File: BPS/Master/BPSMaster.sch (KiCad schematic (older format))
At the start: 21 parts, among them J1 SWD, J13 CAN Analyzer, J5 SPI Analyzer, SW1 B3SL-1002P, U1 STM32F413RHTx, Y1 8M

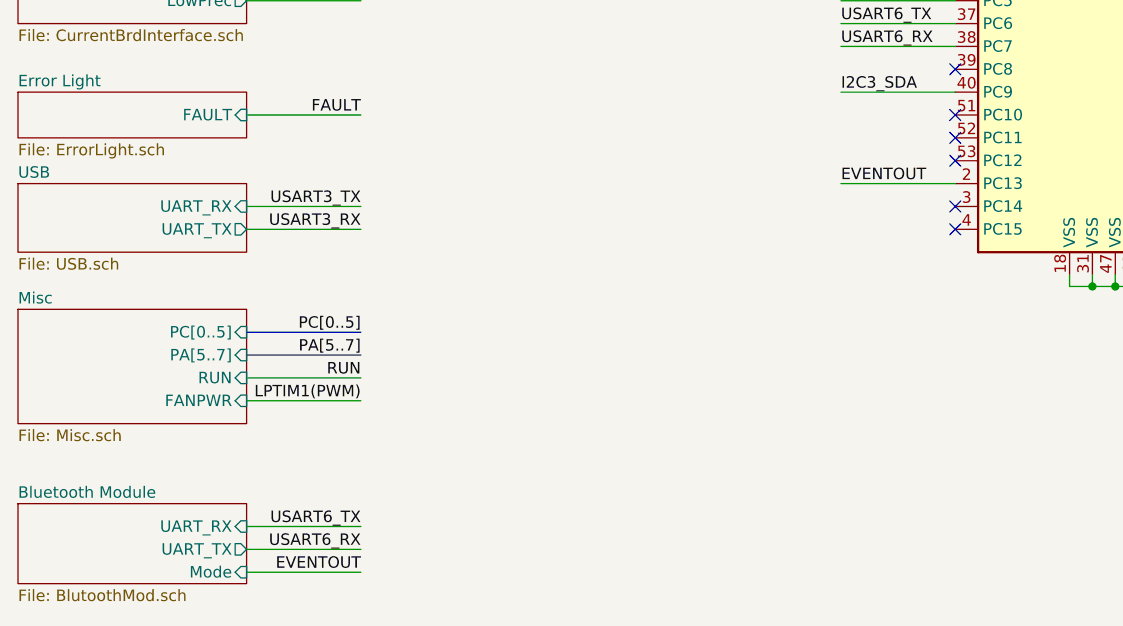
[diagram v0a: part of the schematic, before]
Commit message: The setup for bluetooth mode can't be done through a port using the STM so I used a switch instead, we can use that to toggle between Application mode and testing mode.
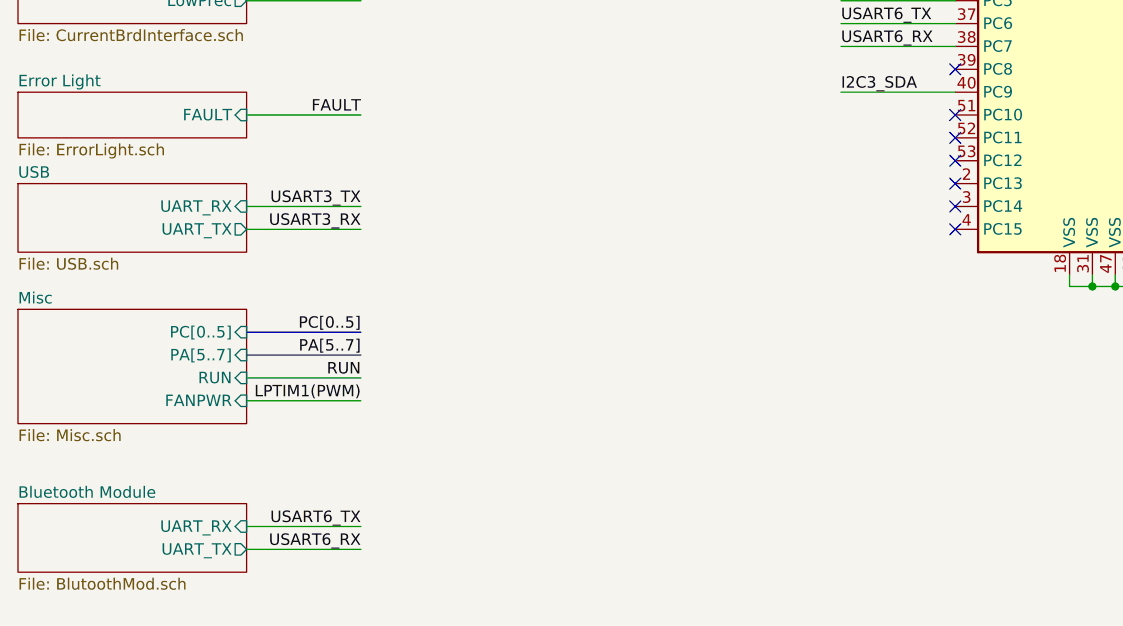
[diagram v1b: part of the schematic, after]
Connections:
- net EVENTOUT: no longer names the net of U1.2 (PC13)
- no-connect marks 19 -> 20
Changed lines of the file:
@@
 USART6_RX
 $Sheet
-S 1000 6700 1000 350
+S 1000 6700 1000 300
 U 5EE39517
 F0 "Bluetooth Module" 50
@@
 F2 "UART_RX" I R 2000 6800 50
 F3 "UART_TX" O R 2000 6900 50
-F4 "Mode" I R 2000 7000 50
 $EndSheet
 Wire Wire Line
@@
 Wire Wire Line
 	2000 6800 2500 6800
-Wire Wire Line
-	2000 7000 2500 7000
 Text Label 2500 6900 2    50   ~ 0
 USART6_RX
 Text Label 2500 6800 2    50   ~ 0
 USART6_TX
-Wire Wire Line
-	5100 5300 4600 5300
-Text Label 4600 5300 0    50   ~ 0
-EVENTOUT
-Text Label 2500 7000 2    50   ~ 0
-EVENTOUT
 Wire Wire Line
 	5100 4600 4600 4600
@@
 Text Label 2500 6250 2    50   ~ 0
 LPTIM1(PWM)
+NoConn ~ 5100 5300
 Wire Bus Line
 	7100 2700 7100 3000

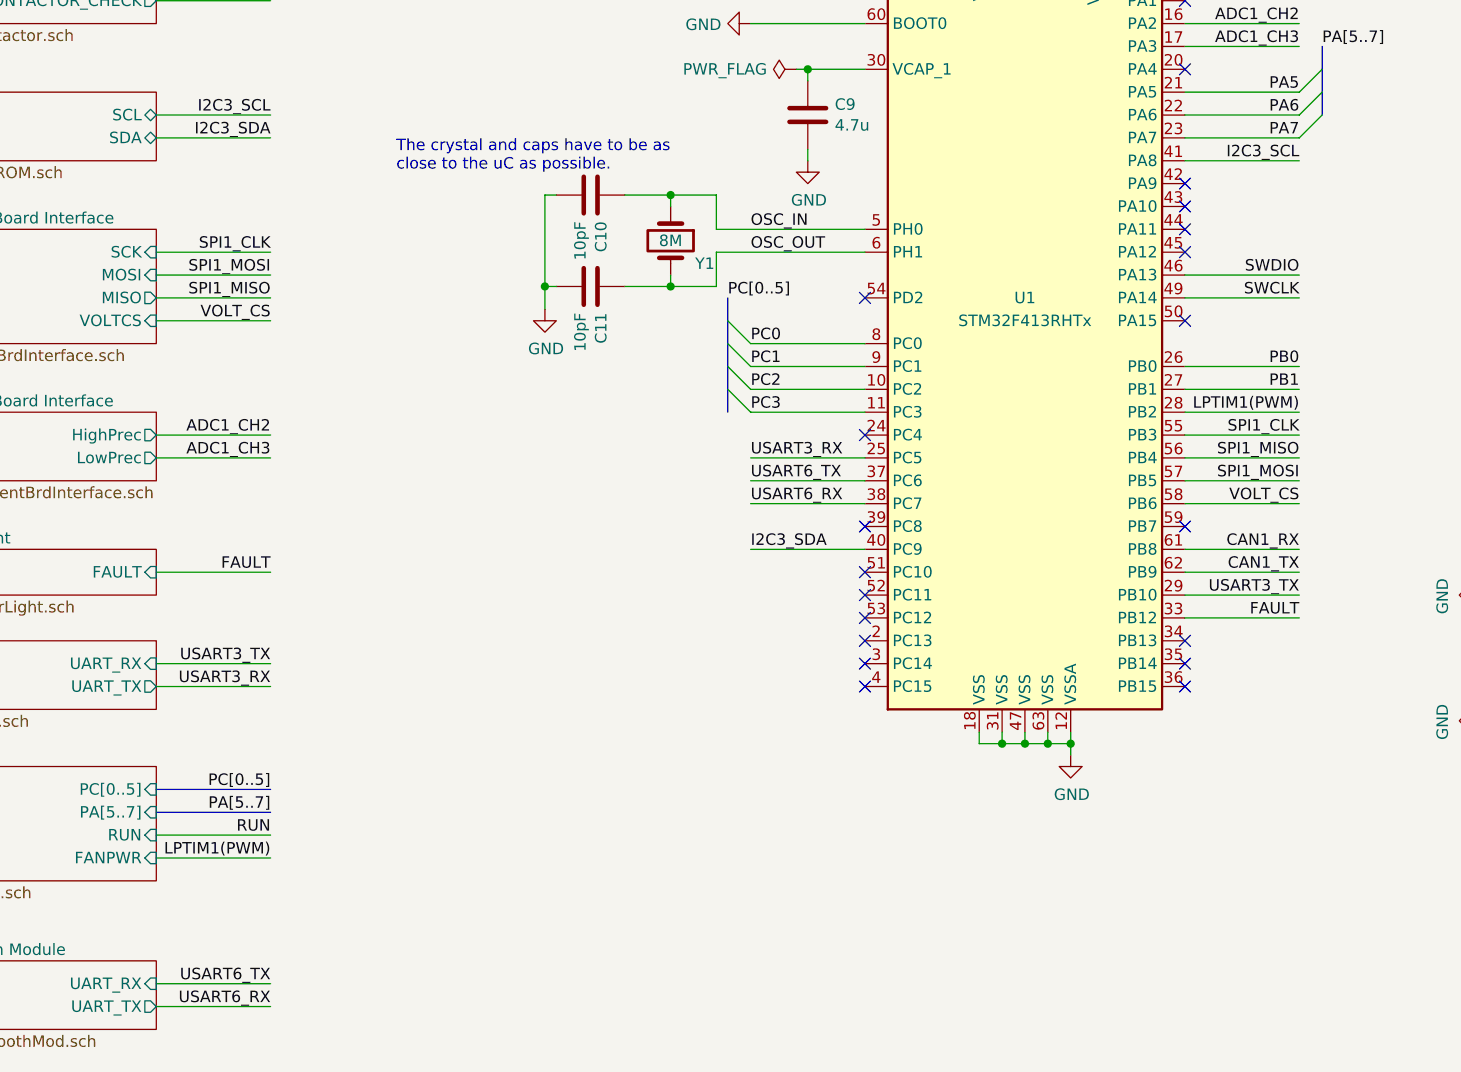
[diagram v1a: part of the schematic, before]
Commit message: Changed UART to UART 1 because it also had CTS and RTS pins
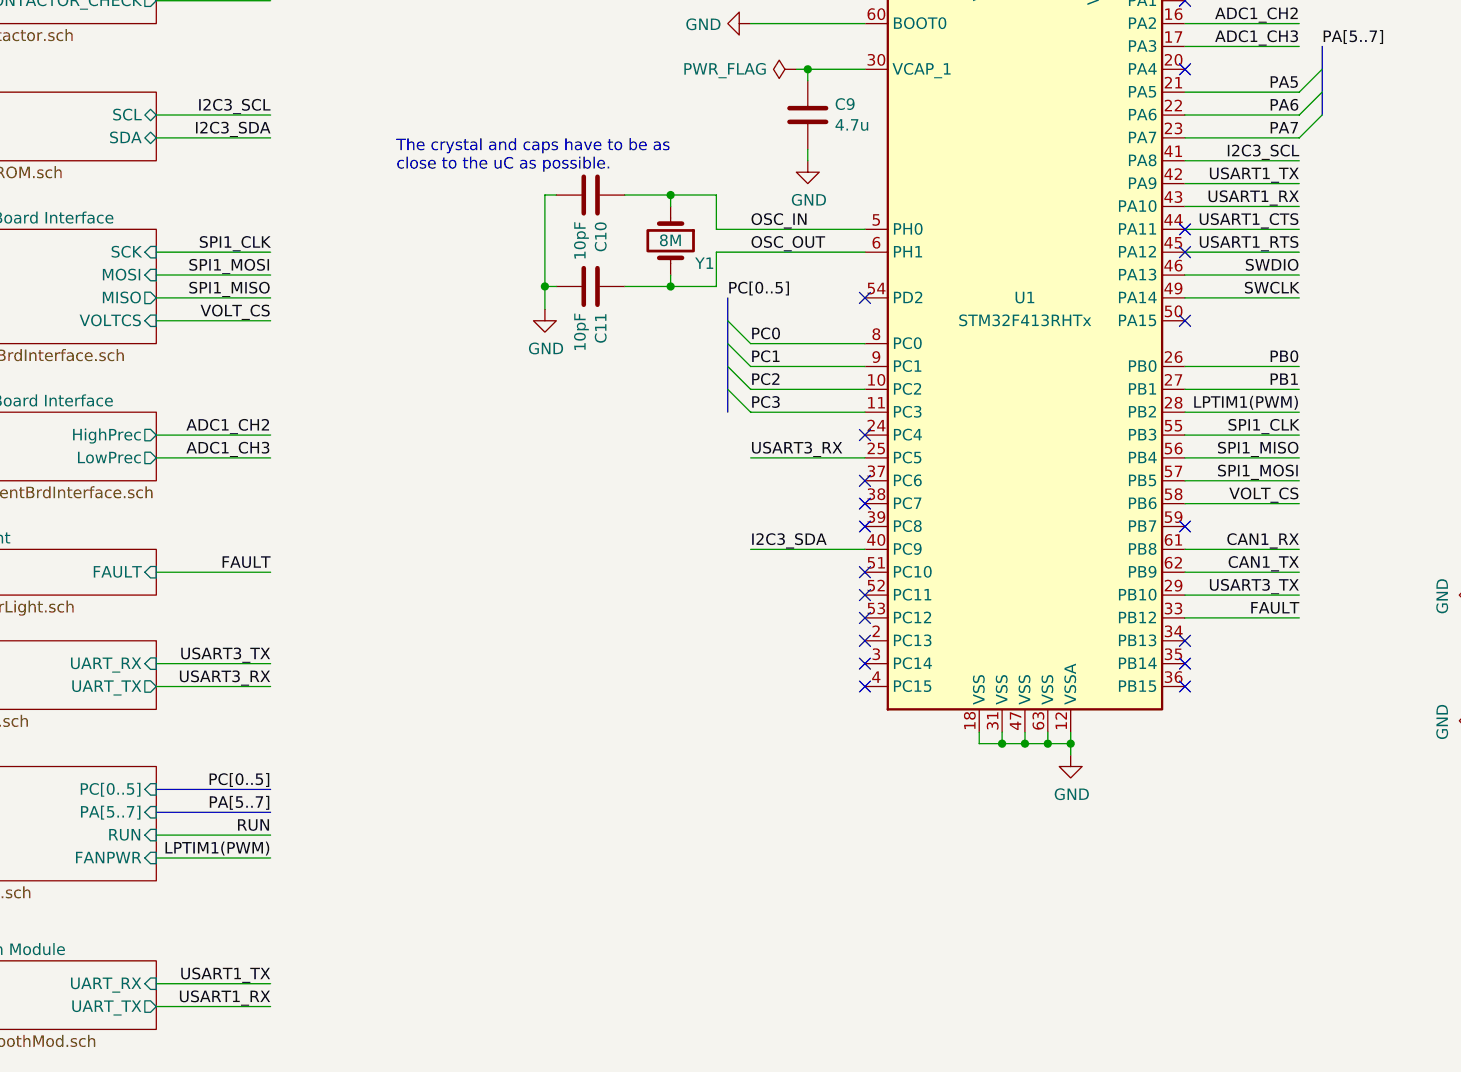
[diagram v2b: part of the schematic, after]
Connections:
- net USART1_TX: now reaches U1.42 (PA9)
- net USART1_RX: now reaches U1.43 (PA10)
- net USART1_CTS: now reaches U1.44 (PA11)
- net USART1_RTS: now reaches U1.45 (PA12)
- net USART6_RX: no longer names the net of U1.38 (PC7)
- net USART6_TX: no longer names the net of U1.37 (PC6)
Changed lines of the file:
@@
 	4800 2800 4850 2800
 Connection ~ 4850 2800
-NoConn ~ 6500 3500
-NoConn ~ 6500 3600
 Wire Wire Line
 	6500 3100 7000 3100
@@
 Wire Wire Line
 	5100 4500 4600 4500
-NoConn ~ 6500 3300
-NoConn ~ 6500 3400
 Wire Wire Line
 	6500 5100 7000 5100
@@
 Text Label 7800 5400 0    50   ~ 0
 SPI1_MOSI
-Wire Wire Line
-	5100 4700 4600 4700
-Text Label 4600 4700 0    50   ~ 0
-USART6_RX
 $Sheet
 S 1000 6700 1000 300
@@
 	2000 6800 2500 6800
 Text Label 2500 6900 2    50   ~ 0
-USART6_RX
+USART1_RX
 Text Label 2500 6800 2    50   ~ 0
-USART6_TX
-Wire Wire Line
-	5100 4600 4600 4600
-Text Label 4600 4600 0    50   ~ 0
-USART6_TX
+USART1_TX
 Wire Wire Line
 	6500 4300 7000 4300
@@
 LPTIM1(PWM)
 NoConn ~ 5100 5300
+Wire Wire Line
+	6500 3300 7000 3300
+Wire Wire Line
+	6500 3400 7000 3400
+Wire Wire Line
+	6500 3500 7000 3500
+Wire Wire Line
+	6500 3600 7000 3600
+Text Label 7000 3300 2    50   ~ 0
+USART1_TX
+Text Label 7000 3400 2    50   ~ 0
+USART1_RX
+Text Label 7000 3500 2    50   ~ 0
+USART1_CTS
+Text Label 7000 3600 2    50   ~ 0
+USART1_RTS
+NoConn ~ 5100 4600
+NoConn ~ 5100 4700
+NoConn ~ 6500 3500
+NoConn ~ 6500 3600
 Wire Bus Line
 	7100 2700 7100 3000

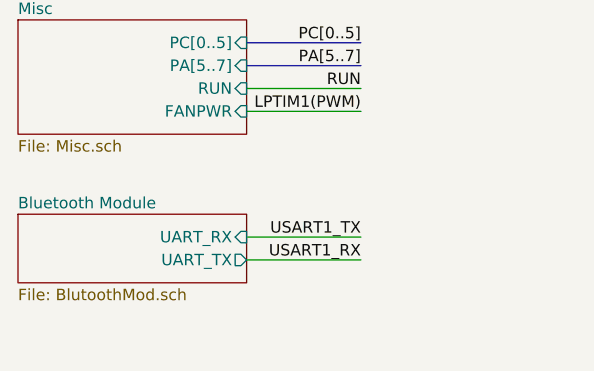
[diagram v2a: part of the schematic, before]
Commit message: Added CTS and RTS connections because we will be sending lots of bytes at a time with the module
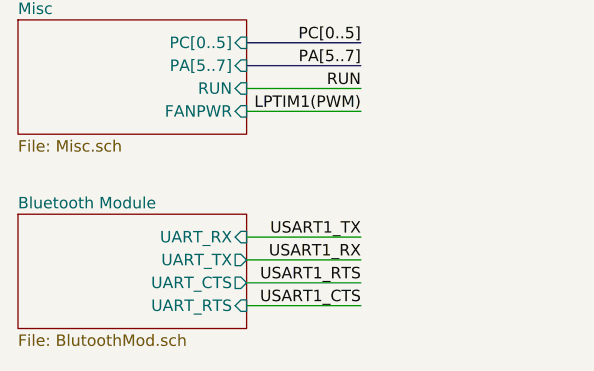
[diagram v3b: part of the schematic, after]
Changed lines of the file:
@@
 SPI1_MOSI
 $Sheet
-S 1000 6700 1000 300
+S 1000 6700 1000 500
 U 5EE39517
 F0 "Bluetooth Module" 50
@@
 F2 "UART_RX" I R 2000 6800 50
 F3 "UART_TX" O R 2000 6900 50
+F4 "UART_CTS" O R 2000 7000 50
+F5 "UART_RTS" I R 2000 7100 50
 $EndSheet
 Wire Wire Line
@@
 NoConn ~ 6500 3500
 NoConn ~ 6500 3600
+Wire Wire Line
+	2000 7000 2500 7000
+Wire Wire Line
+	2000 7100 2500 7100
 Wire Bus Line
 	7100 2700 7100 3000
 Wire Bus Line
 	4500 3800 4500 4300
+Text Label 2500 7000 2    50   ~ 0
+USART1_RTS
+Text Label 2500 7100 2    50   ~ 0
+USART1_CTS
 $EndSCHEMATC

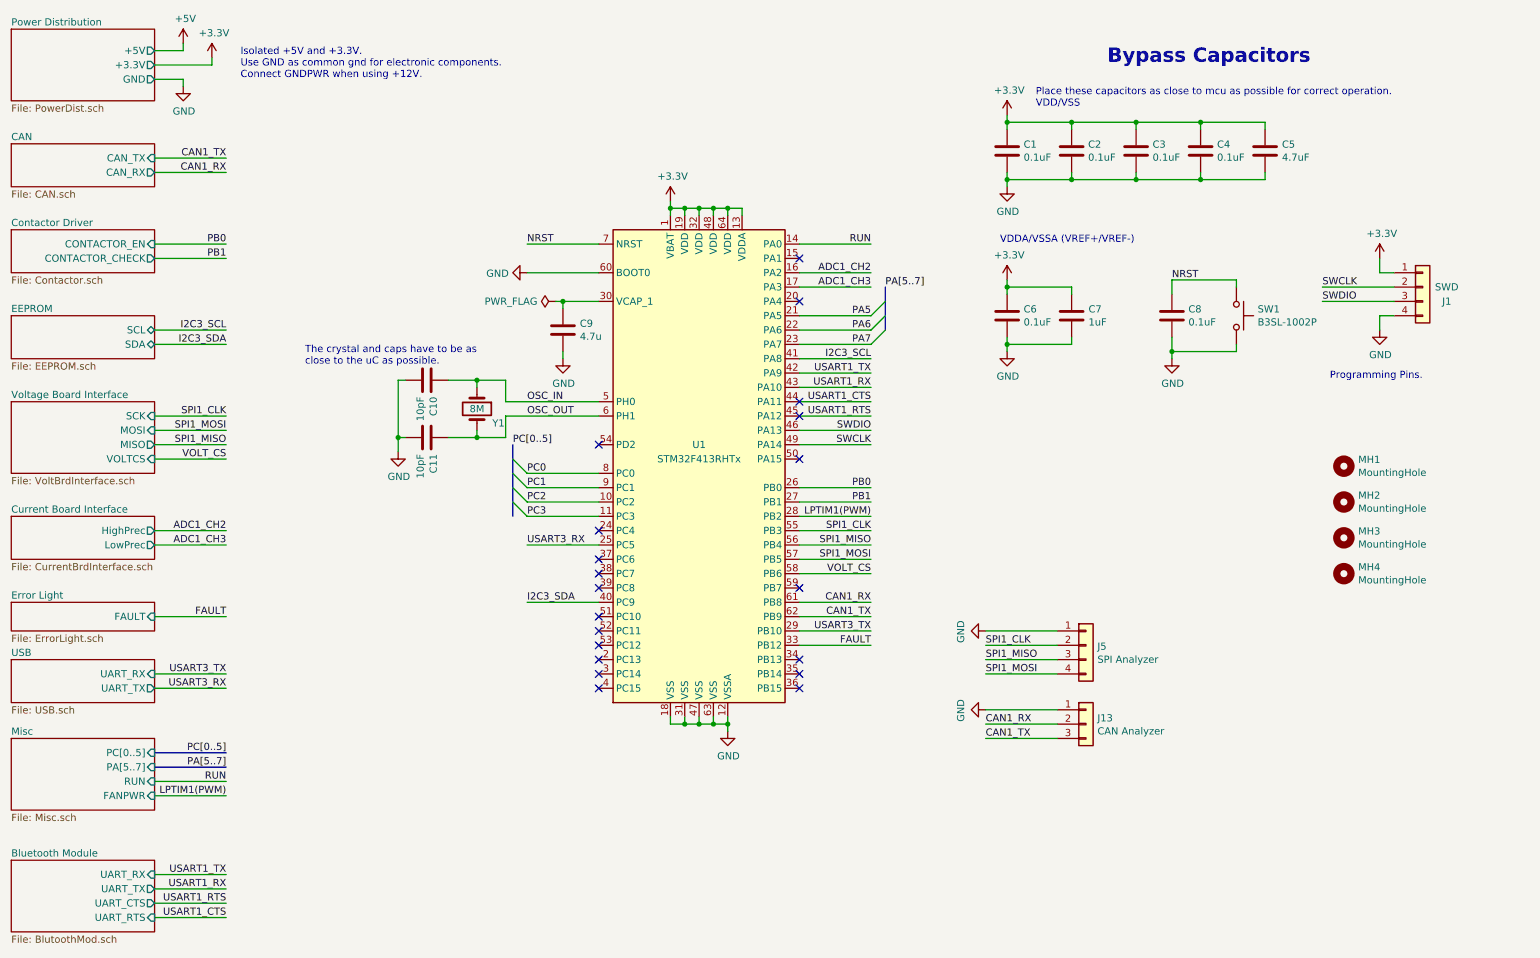
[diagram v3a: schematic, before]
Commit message: Added Interface Pins to Misc sheet so we don't have to make a revision every time we want to add something. Also fixed the input/output for the hierarchial labels.
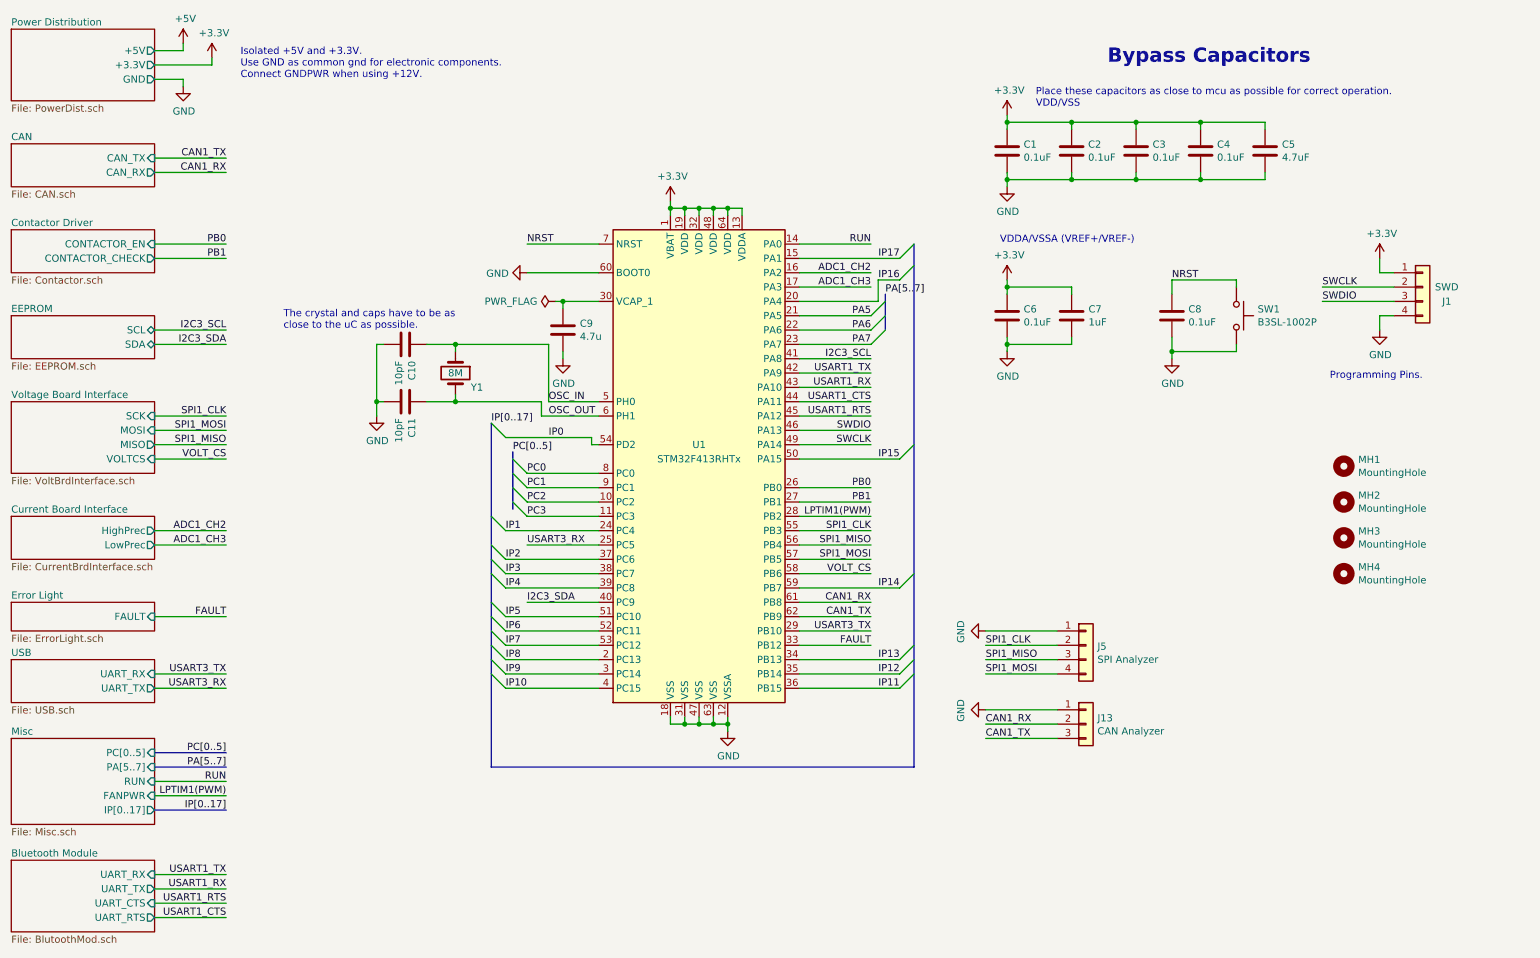
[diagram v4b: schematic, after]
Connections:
- net IP17: now reaches U1.15 (PA1)
- net IP8: now reaches U1.2 (PC13)
- net IP16: now reaches U1.20 (PA4)
- net IP1: now reaches U1.24 (PC4)
- net IP9: now reaches U1.3 (PC14)
- net IP13: now reaches U1.34 (PB13)
- net IP12: now reaches U1.35 (PB14)
- net IP11: now reaches U1.36 (PB15)
- net IP2: now reaches U1.37 (PC6)
- net IP3: now reaches U1.38 (PC7)
- net IP4: now reaches U1.39 (PC8)
- net IP10: now reaches U1.4 (PC15)
- net IP15: now reaches U1.50 (PA15)
- net IP5: now reaches U1.51 (PC10)
- net IP6: now reaches U1.52 (PC11)
- net IP7: now reaches U1.53 (PC12)
- net IP0: now reaches U1.54 (PD2)
- net IP14: now reaches U1.59 (PB7)
- no-connect marks 20 -> 0
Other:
- moved on the sheet: C10, C11, Y1
